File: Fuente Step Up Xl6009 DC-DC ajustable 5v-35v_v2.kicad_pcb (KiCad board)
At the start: 2 copper layers, 7 parts, among them U1 XL6009E1

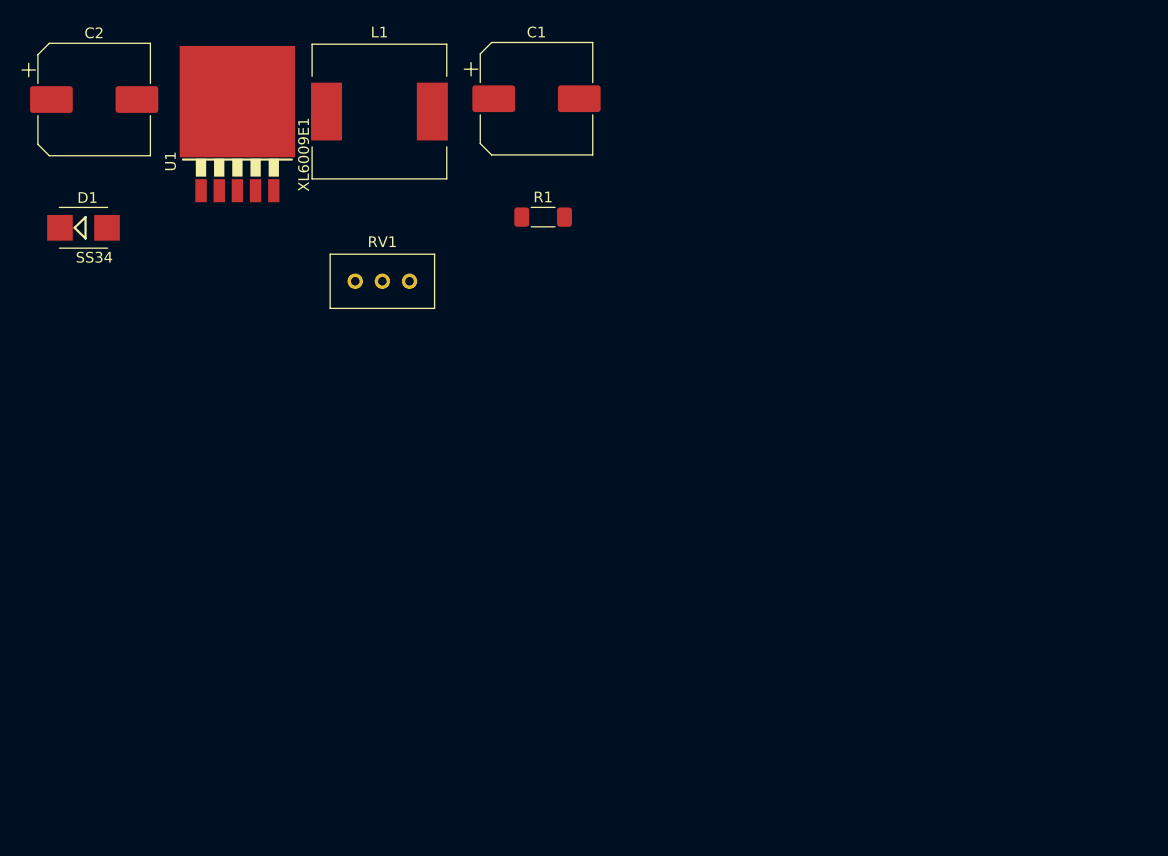
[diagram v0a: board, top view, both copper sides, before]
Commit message: Se creo pcb y se hicieron modificaciones de acuerdo a recomendaciones del docente
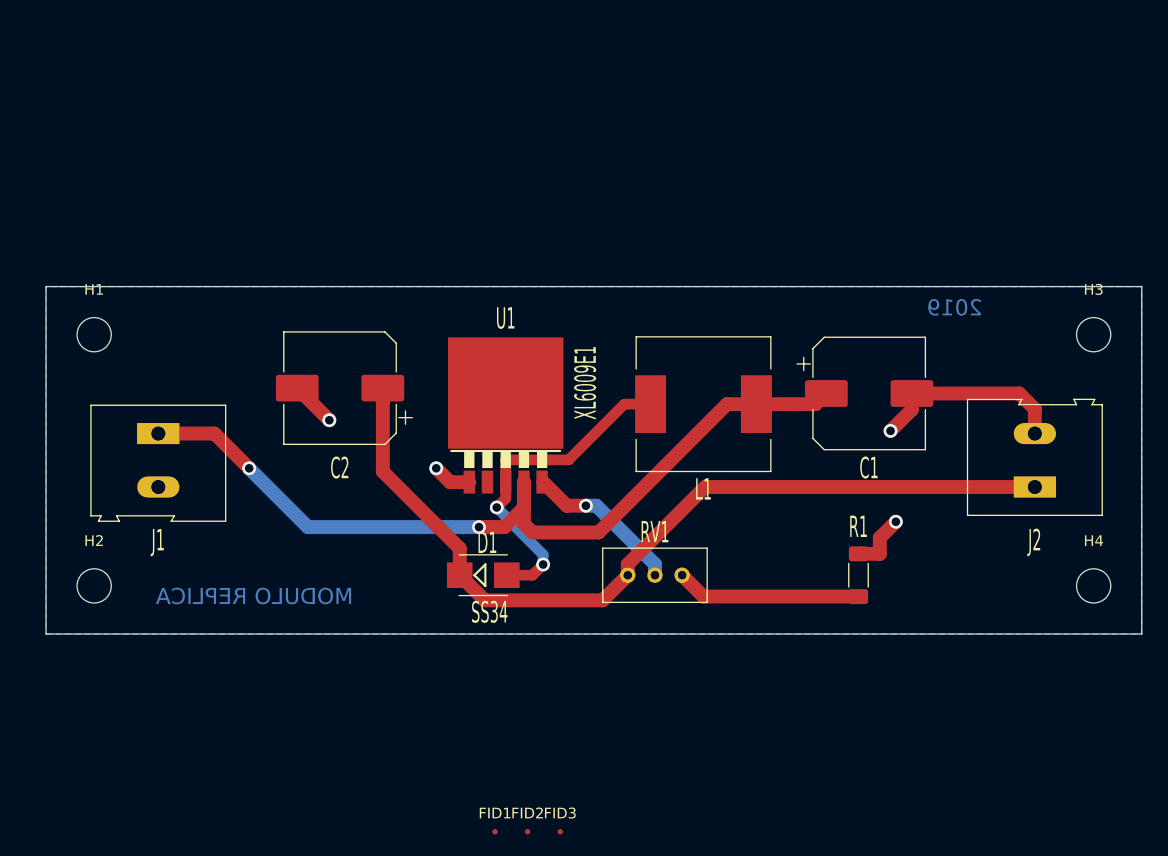
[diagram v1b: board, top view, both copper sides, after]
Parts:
- added FID1: Fiducial, Fiducial:Fiducial_0.5mm_Mask1.5mm, F.Cu at (137.0, 138.5)
- added FID2: Fiducial, Fiducial:Fiducial_0.5mm_Mask1.5mm, F.Cu at (140.1, 138.5)
- added FID3: Fiducial, Fiducial:Fiducial_0.5mm_Mask1.5mm, F.Cu at (143.1, 138.5)
- added H1: MountingHole, MountingHole:MountingHole_3.2mm_M3, F.Cu at (99.5, 92.0)
- added H2: MountingHole, MountingHole:MountingHole_3.2mm_M3, F.Cu at (99.5, 115.5)
- added H3: MountingHole, MountingHole:MountingHole_3.2mm_M3, F.Cu at (193.0, 92.0)
- added H4: MountingHole, MountingHole:MountingHole_3.2mm_M3, F.Cu at (193.0, 115.5)
- added J1: Screw_Terminal_01x02, TerminalBlock:TerminalBlock_Altech_AK300-2_P5.00mm, F.Cu at (105.5, 101.2)
- added J2: Screw_Terminal_01x02, TerminalBlock:TerminalBlock_Altech_AK300-2_P5.00mm, F.Cu at (187.5, 106.2)
- moved D1 49.5 mm to (135.9, 114.5)
- moved R1 44.6 mm to (171.0, 114.5), turned to 90 degrees
- moved C1 41.6 mm to (172.0, 97.5)
- moved L1 40.8 mm to (156.5, 98.5), turned to 180 degrees
- moved RV1 37.5 mm to (154.5, 114.5)
- moved U1 37.1 mm to (138.0, 100.0)
- moved C2 35.5 mm to (122.5, 97.0), turned to 180 degrees
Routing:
- net VCC: track 0.00 -> 80.6 mm, vias 0 -> 2
- net Net-(C2-Pad1): track 0.00 -> 80.2 mm
- net GND: track 0.00 -> 33.2 mm, vias 0 -> 4
- net Net-(D1-PadA): track 0.00 -> 32.7 mm, vias 0 -> 2
- net Net-(R1-Pad1): track 0.00 -> 17.3 mm
- net Net-(RV1-Pad2): track 0.00 -> 14.7 mm, vias 0 -> 1
- added copper zone on B.Cu, net GND
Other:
- board outline added: 102.5 x 32.5 mm
- net class Default: clearance 0.2 -> 0.5; trace_width 0.25 -> 1.3; via_dia 0.8 -> 1.3; via_drill 0.4 -> 0.8
- rule trace_clearance: 0.2 -> 0.5
- board text added: "2019"
- board text added: "MODULO REPLICA"

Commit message: Se modificaron las posiciones de los componentes de acuerdo a la recomencadion del companiero y se rutearon nuevamente algunas pistas
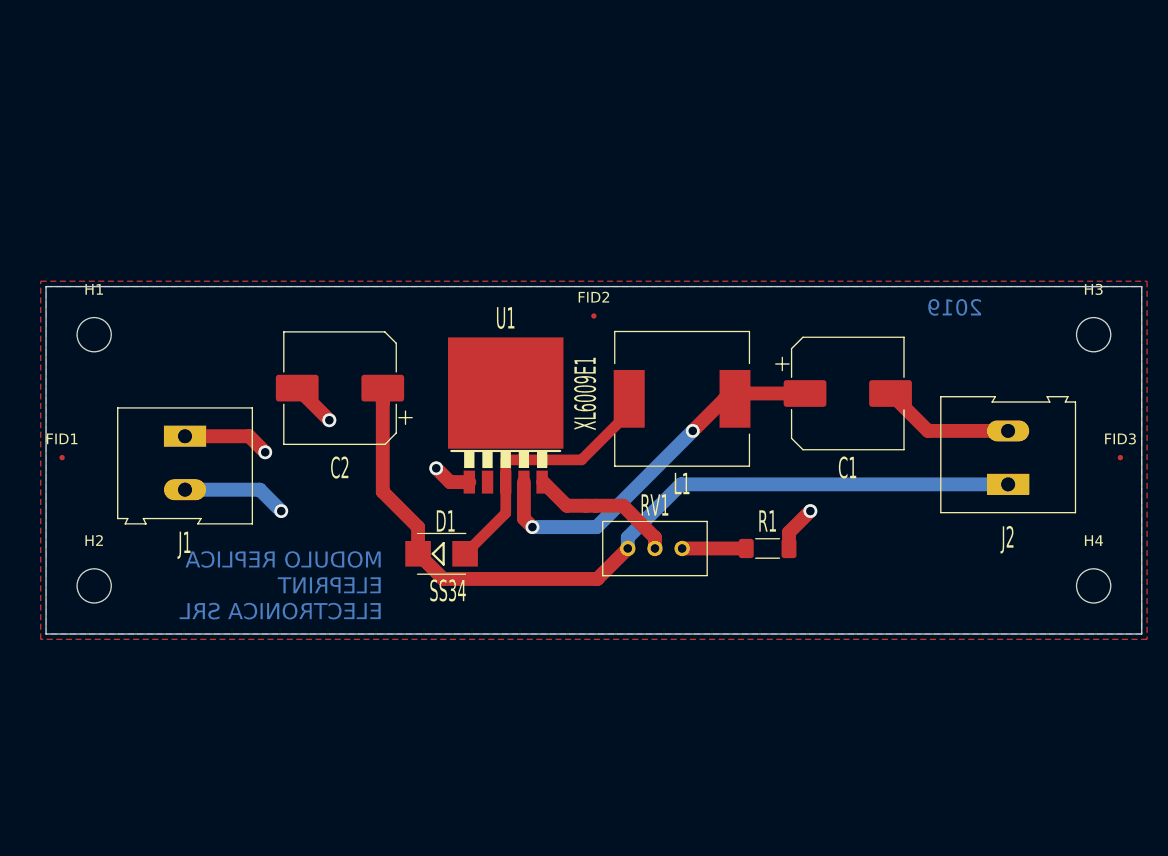
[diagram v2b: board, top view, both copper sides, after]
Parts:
- moved FID3 63.0 mm to (195.5, 103.5)
- moved FID1 53.5 mm to (96.5, 103.5)
- moved FID2 48.6 mm to (146.2, 90.2)
- moved R1 8.86 mm to (162.5, 112.0), turned to 0 degrees
- moved D1 4.38 mm to (132.0, 112.5)
- moved J1 2.51 mm to (108.0, 101.5)
- moved J2 2.51 mm to (185.0, 106.0)
- moved RV1 2.50 mm to (154.5, 112.0)
- moved L1 2.06 mm to (154.5, 98.0)
- moved C1 2.00 mm to (170.0, 97.5)
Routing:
- net VCC: track 80.6 -> 44.3 mm, vias 2 -> 3
- net Net-(R1-Pad1): track 17.3 -> 6.00 mm
- net Net-(D1-PadA): track 32.7 -> 25.0 mm, vias 2 -> 0
- net Net-(C2-Pad1): track 80.2 -> 77.3 mm
- net GND: track 33.2 -> 34.5 mm
- net Net-(RV1-Pad2): track 14.7 -> 13.6 mm, vias 1 -> 0
- added copper zone on F.Cu, net VCC
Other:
- board text added: "Grilla: 0,5 mm Ancho de las pistas: 1,3 mm Ancho de via: 1,30 mm Ancho de agujero: 0,8 mm"
- board text added: "MODULO REPLICA ELEPRINT ELECTRONICA SRL"
- board text removed: "MODULO REPLICA"

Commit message: Se acomodaron componentes y acortaron rutas
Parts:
- moved R1 2.55 mm to (163.0, 109.5)
- moved RV1 2.06 mm to (155.0, 110.0)
- moved D1 1.50 mm to (132.0, 111.0)
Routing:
- net Net-(D1-PadA): track 25.0 -> 23.5 mm
- net Net-(C2-Pad1): track 77.3 -> 78.7 mm, vias 0 -> 2
- net Net-(RV1-Pad2): track 13.6 -> 14.9 mm
- net GND: track 34.5 -> 35.1 mm
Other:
- board text added: "Grilla: 0,5 mm Ancho de las pistas: 1,3 mm Ancho de via: 1,3 mm Ancho de agujero: 0,8 mm"
- board text removed: "Grilla: 0,5 mm Ancho de las pistas: 1,3 mm Ancho de via: 1,30 mm Ancho de agujero: 0,8 mm"
